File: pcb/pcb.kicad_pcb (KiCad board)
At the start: 2 copper layers, 235.2 x 91.7 mm, 96 parts, among them J1 USB_C_Receptacle_USB2.0, Q1 DTC123J, SW1 SW_Push, SW10 SW_PUSH, SW11 SW_PUSH, SW12 SW_PUSH, SW13 SW_PUSH, SW14 SW_PUSH, SW15 SW_PUSH, SW16 SW_PUSH, SW17 SW_PUSH, SW18 SW_PUSH, SW19 SW_PUSH, SW2 SW_PUSH, SW20 SW_PUSH, SW21 SW_PUSH, SW22 SW_PUSH, SW23 SW_PUSH, SW24 SW_PUSH, SW25 SW_PUSH, SW26 SW_PUSH, SW27 SW_PUSH, SW28 SW_PUSH, SW29 SW_PUSH, SW3 SW_PUSH, SW30 SW_PUSH, SW31 SW_PUSH, SW32 SW_PUSH, SW33 SW_PUSH, SW34 Rotary_Encoder_Switch, SW4 SW_PUSH, SW5 SW_PUSH, SW6 SW_PUSH, SW7 SW_PUSH, SW8 SW_PUSH, SW9 SW_PUSH, U1 STM32F072CBTx, U2 MCP1700-3002E_SOT23, U3 SRV05-4

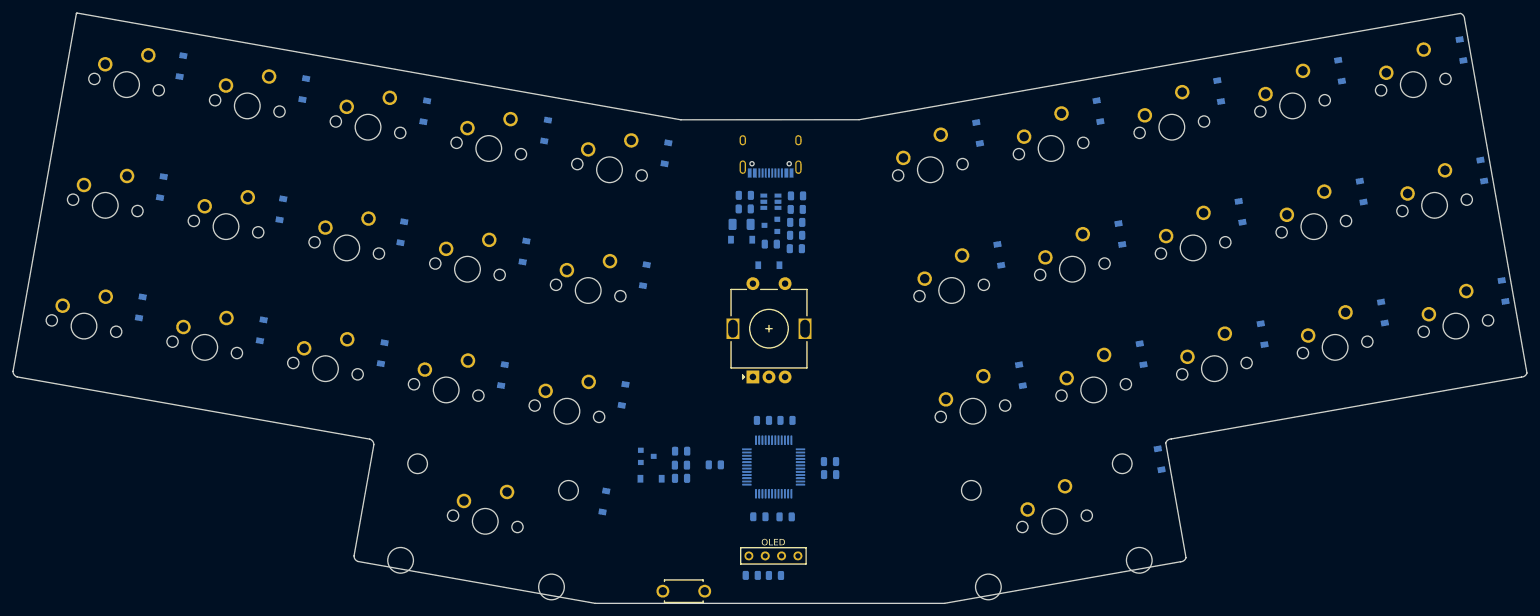
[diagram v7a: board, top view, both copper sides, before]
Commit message: Finishes transition to arm / usb c
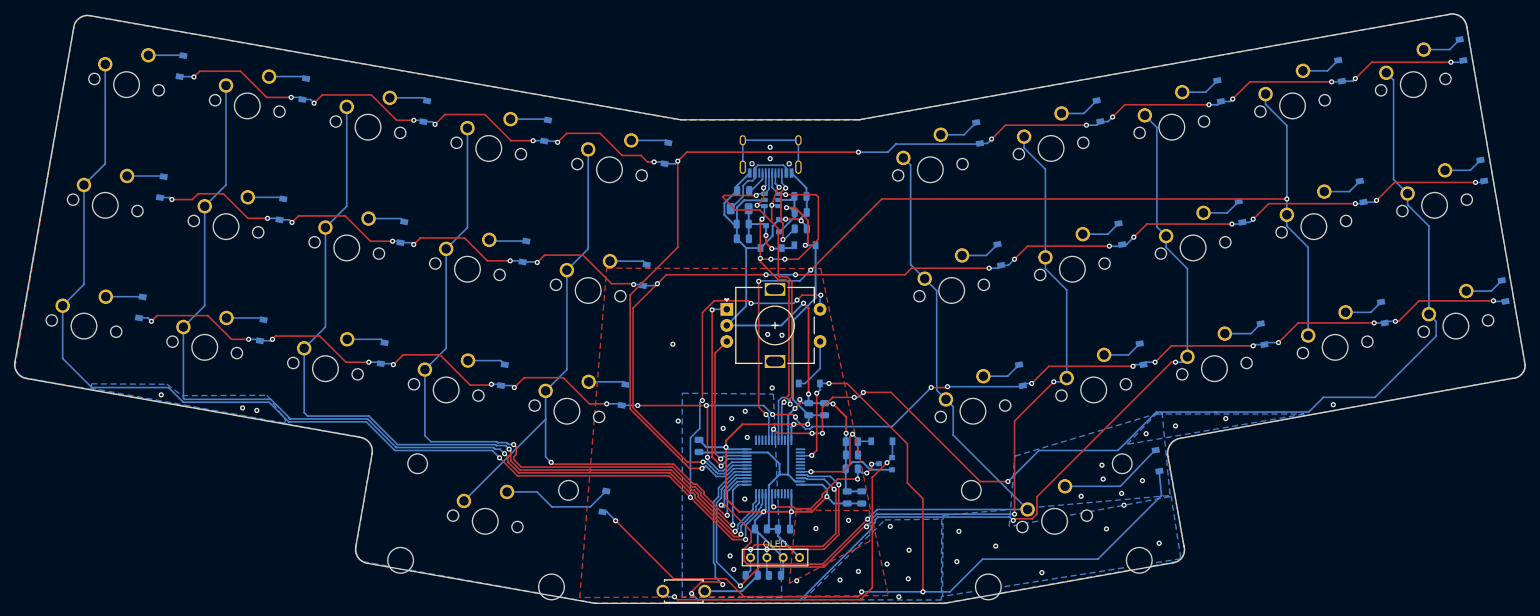
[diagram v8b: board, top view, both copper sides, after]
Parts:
- removed R6, R7: 22, Resistor_SMD:R_0805_2012Metric
- added D36: SMF9.0CA, Diode_SMD:D_SOD-123, B.Cu at (139.1, 108.1)
- D35: value D_Small -> SOD_123
- moved Q1 37.0 mm to (156.9, 141.6), turned to 180 degrees
- moved D35 36.3 mm to (156.3, 138.1), turned to 0 degrees
- moved C10 27.1 mm to (151.6, 138.2)
- moved C11 26.7 mm to (151.6, 142.4), turned to 180 degrees
- moved R3 26.6 mm to (151.7, 140.3)
- moved D33 19.4 mm to (145.0, 129.2), turned to 180 degrees
- moved R5 12.2 mm to (134.8, 99.2), turned to 0 degrees
- moved D34 9.89 mm to (144.3, 107.7), turned to 0 degrees
- moved R1 9.52 mm to (134.7, 106.7), turned to 180 degrees
- moved C8 8.64 mm to (143.6, 100.1)
- moved C9 8.32 mm to (134.7, 104.4), turned to 180 degrees
- moved C5 7.44 mm to (153.2, 146.9), turned to 90 degrees
- moved C2 7.32 mm to (144.9, 133.2), turned to 90 degrees
- moved C1 6.17 mm to (147.4, 133.2), turned to 90 degrees
- moved R4 5.23 mm to (143.7, 105.1)
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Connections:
- F1 pad 2: VBUS -> VCC
- J1 pad A4: VBUS -> VCC
- J1 pad A6: DBUS+ -> D+
- J1 pad A7: DBUS- -> D-
- J1 pad A9: VBUS -> VCC
- J1 pad B4: VBUS -> VCC
- J1 pad B6: DBUS+ -> D+
- J1 pad B7: DBUS- -> D-
- J1 pad B9: VBUS -> VCC
- OL1 pad 3: VDD -> +3V3
- R8 pad 2: VDD -> +3V3
- R9 pad 1: VDD -> +3V3
- U3 pad 1: DBUS- -> D-
- U3 pad 3: DBUS+ -> D+
- U3 pad 4: DBUS- -> D-
- U3 pad 5: VBUS -> +3V3
- U3 pad 6: DBUS+ -> D+
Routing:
- net row0: track 0.00 -> 280.8 mm, vias 0 -> 19
- net row1: track 0.00 -> 265.1 mm, vias 0 -> 21
- net row2: track 0.00 -> 247.8 mm, vias 0 -> 23
- net col0: track 0.00 -> 226.0 mm, vias 0 -> 7
- net col9: track 0.00 -> 169.5 mm, vias 0 -> 6
- net GND: track 0.00 -> 165.1 mm, vias 0 -> 38
- net col7: track 0.00 -> 163.1 mm, vias 0 -> 4
- net row3: track 0.00 -> 157.7 mm, vias 0 -> 6
- net col1: track 0.00 -> 155.2 mm, vias 0 -> 2
- net +3V3: track 0.00 -> 153.7 mm, vias 0 -> 8
- net col8: track 0.00 -> 153.0 mm, vias 0 -> 4
- net col6: track 0.00 -> 135.6 mm, vias 0 -> 4
- net col2: track 0.00 -> 133.7 mm, vias 0 -> 2
- net col5: track 0.00 -> 129.2 mm, vias 0 -> 2
- net col3: track 0.00 -> 114.5 mm, vias 0 -> 2
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- added copper zone on B.Cu, net GND
- added copper zone on F.Cu, net GND
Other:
- board size 235.2 x 91.7 mm -> 234.7 x 91.6 mm
- net class Power: trace_width 0.381 -> 0.3
